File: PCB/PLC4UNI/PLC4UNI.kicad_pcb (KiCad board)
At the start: 4 copper layers, 102.4 x 83.1 mm, 207 parts, among them J1 Conn_02x08_Odd_Even, K1 G5V-1-DC3, K2 G5V-1-DC3, Q1 ZXMS6004FFQTA, Q2 ZXMS6004FFQTA, Q3 ZXMS6004FFQTA, Q4 ZXMS6004FFQTA, Q5 NCE60P04R, SW1 TS-1088-AR02016, SW2 TS-1088-AR02016, U1 ScrewTerminal1-1x9-P5.0mm, U10 AT3H4B-CUH-S, U11 AT3H4B-CUH-S, U12 AT3H4B-CUH-S, U13 AT3H4B-CUH-S, U14 AT3H4B-CUH-S, U15 MAX31856MUD+, U16 GP8211S-TC50-EW, U17 GP8302-TC50-EW, U18 BL0942, U19 B0303S-1WR3_C7465185, U2 ScrewTerminal1-1x9-P5.0mm, U20 ISO7021DR, U21 AP63203WU-7, U22 APH0630T4R7M, U23 TD301M485_C5451847, U3 ScrewTerminal1-1x9-P5.0mm, U4 ScrewTerminal1-1x9-P5.0mm, U5 ADS1115IDGS, U6 ESP32-S3-WROOM-1, U7 BTS723GWXUMA1, U8 LK1802, U9 AT3H4B-CUH-S

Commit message: 0-10V input, 4-20mA input
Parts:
- D13, D15: value 1N5819 -> 1N5819HW-7-F; footprint PCM_Diode_THT_AKL:D_DO-41_SOD81_P7.62mm_Horizontal -> EasyEDA:SOD-123_L2.7-W1.6-LS3.7-RD
- moved TP5 412.6 mm to (270.2, 95.9)
- moved TP6 412.6 mm to (270.2, 102.0)
- moved R61 387.6 mm to (245.9, 95.7), turned to -90 degrees
- moved U19 385.1 mm to (254.3, 113.4), turned to 90 degrees
- moved R63 384.3 mm to (252.7, 86.4)
- moved R66 383.9 mm to (252.7, 88.4), turned to 180 degrees
- moved R62 383.4 mm to (241.9, 95.7), turned to 90 degrees
- moved C34 382.8 mm to (244.9, 98.7)
- moved C38 381.7 mm to (244.7, 101.9)
- moved R67 380.5 mm to (252.7, 90.4)
- moved R68 380.5 mm to (252.7, 92.4), turned to 180 degrees
- moved R69 380.4 mm to (252.7, 94.4)
- moved R70 380.4 mm to (252.7, 96.4), turned to 180 degrees
- moved C37 380.1 mm to (241.4, 111.9), turned to 180 degrees
- moved C36 378.6 mm to (240.9, 101.9)
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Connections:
- C5 pad 2: /plc4uni_top/CON_IN_4-20MA_1 -> GND
- C6 pad 2: /plc4uni_top/CON_IN_4-20MA_1 -> GND
- C7 pad 2: /plc4uni_top/CON_IN_4-20MA_2 -> GND
- C8 pad 2: /plc4uni_top/CON_IN_4-20MA_2 -> GND
- D13 pad 2: /plc4uni_top/CON_IN_4-20MA_1 -> GND
- D14 pad 2: /plc4uni_top/CON_IN_4-20MA_1 -> GND
- D15 pad 2: /plc4uni_top/CON_IN_4-20MA_2 -> GND
- D16 pad 2: /plc4uni_top/CON_IN_4-20MA_2 -> GND
- D34 pad 1: (no net) -> GND
- D34 pad 2: (no net) -> Net-(JP1-A)
- R15 pad 1: /plc4uni_top/IN-4-20MA/IN_P -> /plc4uni_top/CON_IN_4-20MA_1
- R16 pad 1: /plc4uni_top/CON_IN_4-20MA_1 -> GND
- R19 pad 1: /plc4uni_top/IN-4-20MA1/IN_P -> /plc4uni_top/CON_IN_4-20MA_2
- R20 pad 1: /plc4uni_top/CON_IN_4-20MA_2 -> GND
- U15 pad 14: unconnected-(U15-DGND-Pad14) -> GND
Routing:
- net GND: track 34.9 -> 64.0 mm, vias 31 -> 48
- net Net-(U18-VP): track 0.00 -> 25.4 mm, vias 0 -> 1
- net VCC: track 80.9 -> 58.1 mm, vias 6 -> 5
- net /plc4uni_top/CON_IN_PNP2: track 30.9 -> 8.67 mm
- net /plc4uni_top/IN-4-20MA1/OUT: track 0.00 -> 18.3 mm, vias 0 -> 2
- net /plc4uni_top/CON_IN_PNP1: track 26.3 -> 8.22 mm
- net Earth: track 0.00 -> 17.9 mm, vias 0 -> 8
- net /plc4uni_top/CON_IN_TC+: track 28.3 -> 11.4 mm
- net /plc4uni_top/IN-0-10V1/OUT3V3: track 0.00 -> 16.2 mm
- net /plc4uni_top/IN-0-10V/OUT3V3: track 0.00 -> 14.6 mm
- net 3.3V: track 21.0 -> 35.3 mm, vias 18 -> 23
- net /plc4uni_top/CON_IN_NPN4: track 21.2 -> 8.08 mm
- net 3.3V_P: track 0.00 -> 12.0 mm, vias 0 -> 4
- net /plc4uni_top/CON_IN_NPN3: track 19.3 -> 7.59 mm
- net /plc4uni_top/IN-4-20MA/OUT: track 0.00 -> 11.4 mm
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- added copper zone on In1.Cu, net 3.3V_P
- added copper zone on B.Cu, net Earth

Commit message: power supply and inputs routed
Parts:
- added H1: MountingHole, MountingHole:MountingHole_2.2mm_M2_DIN965, F.Cu at (252.2, 101.9)
- added H2: MountingHole, MountingHole:MountingHole_2.2mm_M2_DIN965, F.Cu at (179.4, 143.2)
- C5, C7: footprint PCM_Capacitor_SMD_AKL:C_0603_1608Metric -> TestPoint:TestPoint_THTPad_D1.5mm_Drill0.7mm
- TP1, TP2, TP3, TP4, TP5, TP6, TP7: footprint TestPoint:TestPoint_Pad_D4.0mm -> TestPoint:TestPoint_THTPad_D1.5mm_Drill0.7mm
- moved TP7 393.4 mm to (251.2, 105.9)
- moved C39 380.7 mm to (242.4, 115.2), turned to 90 degrees
- moved R73 367.8 mm to (240.9, 120.2), turned to -90 degrees
- moved R74 365.4 mm to (238.9, 120.2), turned to -90 degrees
- moved TP2 328.9 mm to (233.2, 112.7)
- moved TP1 326.7 mm to (228.2, 112.7)
- moved TP3 317.2 mm to (222.4, 113.9)
- moved TP4 311.6 mm to (218.9, 113.9)
- moved R10 289.1 mm to (167.9, 153.2), turned to -90 degrees
- moved D8 286.2 mm to (167.9, 156.4), turned to 90 degrees
- moved R9 285.7 mm to (163.7, 152.9), turned to -90 degrees
- moved U7 284.7 mm to (166.4, 145.9), turned to 90 degrees
- moved D7 283.0 mm to (163.9, 156.1), turned to 90 degrees
- moved R12 274.9 mm to (179.2, 156.2), turned to -90 degrees
- moved Q2 274.6 mm to (177.9, 152.4), turned to 90 degrees
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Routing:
- net VCC: track 58.1 -> 135.0 mm, vias 5 -> 8
- net /plc4uni_top/CON_OUT_PNP2: track 0.00 -> 22.7 mm
- net /plc4uni_top/CON_OUT_PNP1: track 0.00 -> 18.9 mm
- net /plc4uni_top/CON_OUT_NPN2: track 0.00 -> 11.3 mm
- net /plc4uni_top/CON_OUT_NPN1: track 0.00 -> 10.7 mm
- net /plc4uni_top/CON-IN_CT_N: track 2.04 -> 12.0 mm
- net Net-(U18-IN): track 8.18 -> 17.8 mm
- net /plc4uni_top/CON-IN_CT_P: track 2.04 -> 10.8 mm
- net 3.3V: track 35.3 -> 43.5 mm, vias 23 -> 27
- net Net-(U18-IP): track 8.85 -> 14.3 mm
- net GND: track 64.0 -> 68.6 mm, vias 48 -> 51
- net Earth: track 17.9 -> 20.8 mm, vias 8 -> 10
- net Net-(D10-A): track 0.00 -> 2.27 mm
- net Net-(D9-A): track 0.00 -> 2.02 mm
- net Net-(U18-VP): track 25.4 -> 23.7 mm
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
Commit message: ruteo terminado
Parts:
- moved R58 373.3 mm to (252.7, 143.1), turned to 90 degrees
- moved R59 362.7 mm to (240.5, 150.9), turned to -90 degrees
- moved D28 361.9 mm to (241.3, 145.5), turned to -90 degrees
- moved U17 357.8 mm to (246.6, 141.1), turned to 180 degrees
- moved Q5 356.6 mm to (234.3, 146.1)
- moved C32 356.0 mm to (250.4, 143.1), turned to 90 degrees
- moved D29 351.1 mm to (234.9, 153.7), turned to 90 degrees
- moved C31 349.1 mm to (244.5, 135.5), turned to 90 degrees
- moved D30 346.2 mm to (230.9, 155.9), turned to 90 degrees
- moved C33 345.6 mm to (238.3, 150.9), turned to -90 degrees
- moved R60 341.0 mm to (230.9, 151.7), turned to 90 degrees
- moved D36 337.3 mm to (203.9, 152.7), turned to 90 degrees
- moved D35 334.7 mm to (197.4, 155.7)
- moved U6 330.9 mm to (219.2, 126.7), turned to -90 degrees
- moved K2 329.5 mm to (225.4, 151.2), turned to -90 degrees
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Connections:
- C2 pad 1: /plc4uni_top/IN_PNP1 -> /plc4uni_top/IN_PNP2
- D1 pad 1: /plc4uni_top/IN_PNP1 -> /plc4uni_top/IN_PNP2
- K1 pad 9: Net-(U8-1C) -> Net-(U8-2C)
- K2 pad 9: Net-(U8-2C) -> Net-(U8-1C)
- SW2 pad 2: /plc4uni_top/IN_PNP1 -> /plc4uni_top/IN_PNP2
- U6 pad 10: /plc4uni_top/I2C_SDA -> /plc4uni_top/I2C_SCK
- U6 pad 11: /plc4uni_top/I2C_SCK -> /plc4uni_top/I2C_SDA
- U6 pad 15: /plc4uni_top/IN_NPN4 -> /plc4uni_top/OUT_NPN3
- U6 pad 16: /plc4uni_top/IN_PNP1 -> /plc4uni_top/IN_PNP2
- U6 pad 17: /plc4uni_top/RS485-TX -> /plc4uni_top/IN_PNP1
- U6 pad 22: /plc4uni_top/IN_NPN1 -> /plc4uni_top/OUT_NPN4
- U6 pad 24: /plc4uni_top/IN_PNP2 -> /plc4uni_top/RS485-TX
- U6 pad 38: /plc4uni_top/IN_NPN3 -> /plc4uni_top/OUT_NPN2
- U6 pad 39: /plc4uni_top/IN_NPN2 -> /plc4uni_top/OUT_NPN1
- U6 pad 4: /plc4uni_top/OUT_NPN1 -> /plc4uni_top/IN_NPN1
- U6 pad 5: /plc4uni_top/OUT_NPN2 -> /plc4uni_top/IN_NPN2
- U6 pad 6: /plc4uni_top/OUT_NPN3 -> /plc4uni_top/IN_NPN3
- U6 pad 7: /plc4uni_top/OUT_NPN4 -> /plc4uni_top/IN_NPN4
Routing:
- net VCC: track 135.0 -> 256.8 mm, vias 8 -> 6
- net /plc4uni_top/I2C_SCK: track 0.00 -> 112.3 mm, vias 0 -> 3
- net /plc4uni_top/I2C_SDA: track 0.00 -> 110.5 mm, vias 0 -> 3
- net /plc4uni_top/OUT_PNP1: track 0.00 -> 76.2 mm, vias 0 -> 2
- net /plc4uni_top/RESET: track 0.00 -> 72.8 mm, vias 0 -> 3
- net /plc4uni_top/OUT_PNP2: track 0.00 -> 71.1 mm, vias 0 -> 2
- net /plc4uni_top/IN_NPN1: track 5.79 -> 69.2 mm, vias 0 -> 2
- net /plc4uni_top/OUT_NPN1: track 0.00 -> 61.6 mm, vias 0 -> 2
- net /plc4uni_top/IN_PNP2: track 6.04 -> 64.7 mm, vias 0 -> 2
- net /plc4uni_top/OUT_NPN2: track 0.00 -> 55.7 mm, vias 0 -> 2
- net /plc4uni_top/TP_INT: track 0.00 -> 55.7 mm, vias 0 -> 1
- net /plc4uni_top/LCD_CS: track 0.00 -> 53.9 mm, vias 0 -> 2
- net /plc4uni_top/OUT-PNP/ST1: track 0.00 -> 53.4 mm, vias 0 -> 2
- net /plc4uni_top/ST1_ST2: track 0.00 -> 53.4 mm, vias 0 -> 2
- net /plc4uni_top/IN_NPN2: track 5.69 -> 58.6 mm, vias 0 -> 2
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
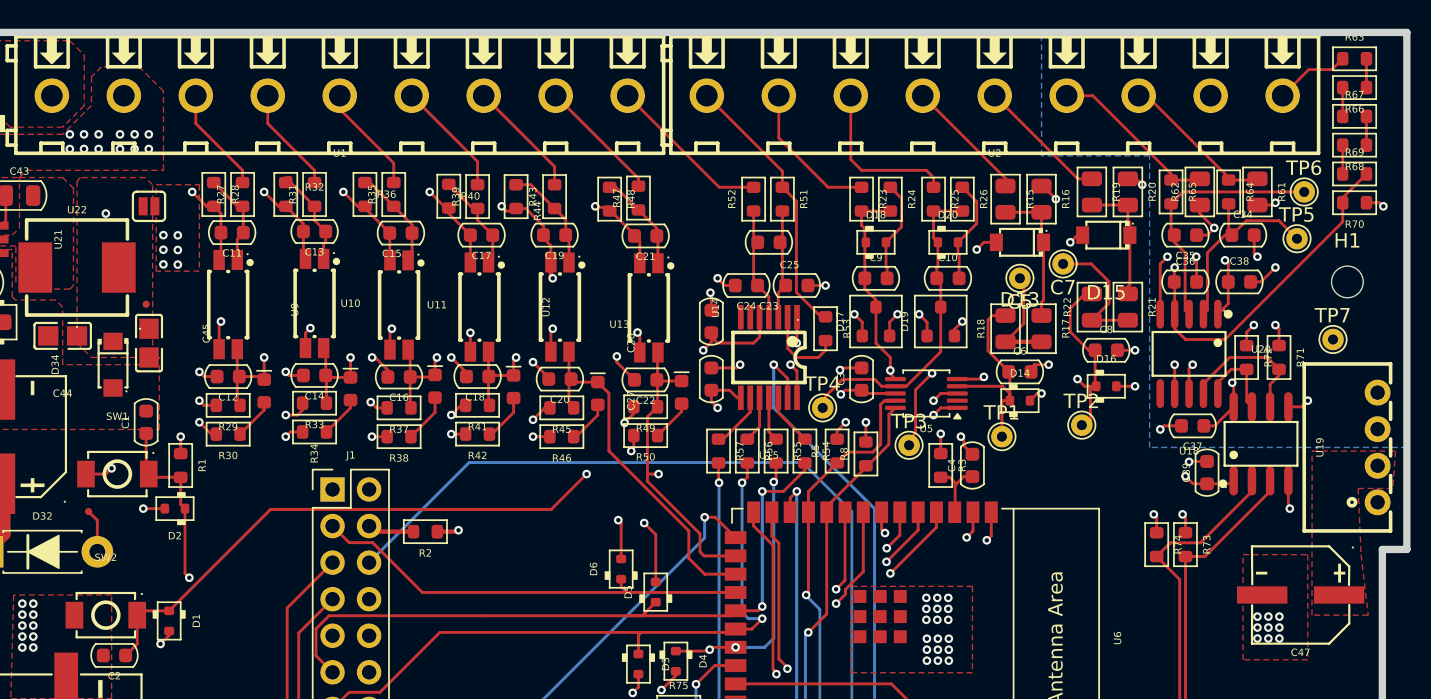
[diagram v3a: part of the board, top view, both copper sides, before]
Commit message: add teardrops
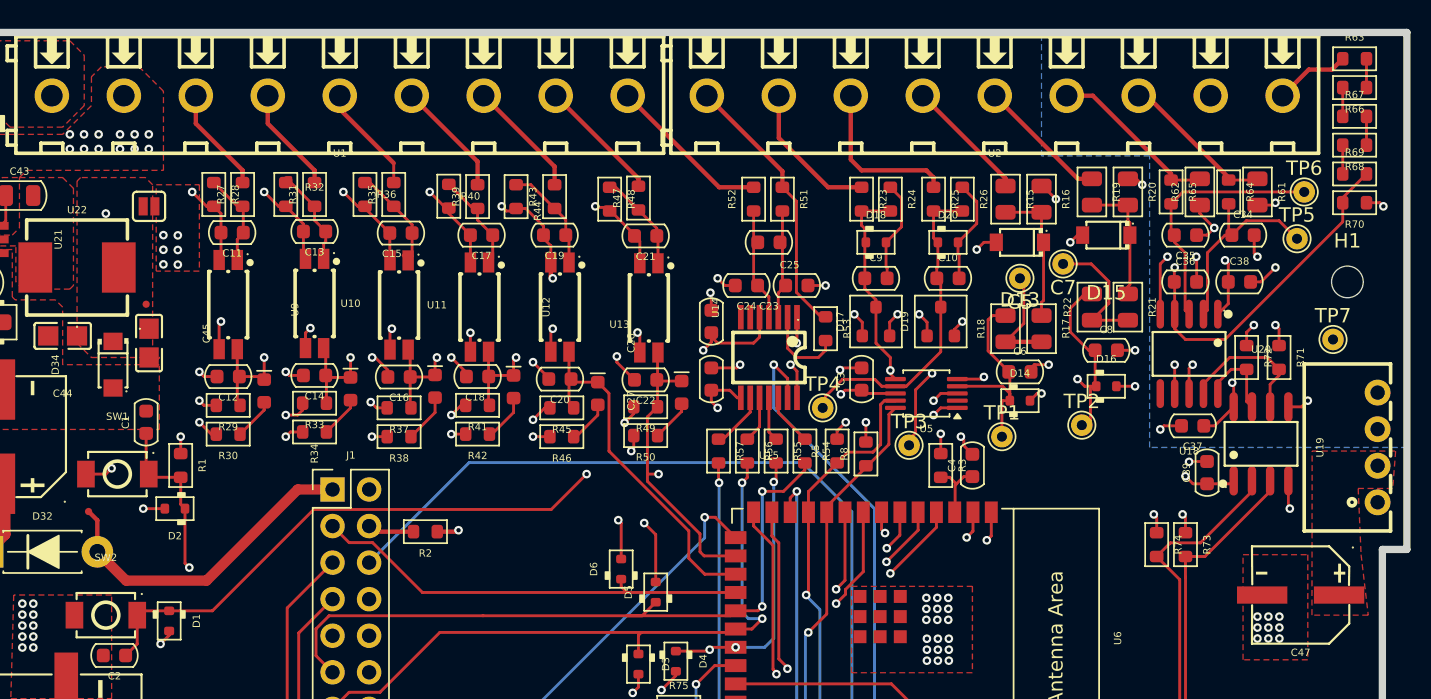
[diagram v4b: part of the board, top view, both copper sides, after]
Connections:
- D32 pad 2: 5V -> +5V
- TP8 pad 1: 5V -> +5V
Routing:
- net +5V: track 0.00 -> 22.8 mm
- net 5V: track 3.05 -> 0.00 mm
- net /plc4uni_top/RESET: track 72.8 -> 71.8 mm

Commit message: add mezzanini pcb
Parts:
- U6: footprint Espressif:ESP32-S3-WROOM-1 -> Espressif:ESP32-S3-WROOM-1U
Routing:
- net VCC: track 256.8 -> 255.8 mm
